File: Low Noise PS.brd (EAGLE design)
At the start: 228.6 x 101.6 mm, 64 parts, among them IC1 MAX6350SO08, IC2 OP27, IC3 LT1677, IC4 LT1677, IC5 MC79M12CDTG, IC6 MC78M12BDTG, Q1 MMBT2907AMMBTA56SOT23, Q2 MMBT5550SOT23, Q3 PMBF170, Q4 BSH201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

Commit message: Almost ready to print
1) "cosmetic" adjustments needed (mainly increasing clearance for traces
below SMD parts)
2) component values need to be adjusted and chosen
3) Silkscreen needs to be cleaned
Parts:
- added C26, C27, C28, C29: 22uF, rlc-jqi:1206
- added F1, F2: (no value), jqi-power-supply:FUSE1206
- moved R7 255.4 mm to (193.5, 41.5), turned to 90 degrees
- moved C7 245.1 mm to (200.0, 41.3)
- moved R2 243.3 mm to (205.4, 39.4)
- moved T1 241.9 mm to (187.7, 26.2), turned to 90 degrees
- moved C20 240.4 mm to (197.6, 41.3), turned to 270 degrees
- moved IC3 239.7 mm to (199.2, 35.6)
- moved R10 238.3 mm to (193.9, 35.4), turned to 90 degrees
- moved R1 238.0 mm to (206.8, 35.3), turned to 0 degrees
- moved C14 237.4 mm to (196.1, 28.6), turned to 270 degrees
- moved R9 236.2 mm to (192.7, 18.2), turned to 270 degrees
- moved R12 236.0 mm to (198.9, 28.6), turned to 90 degrees
- moved C11 235.8 mm to (201.9, 28.6), turned to 270 degrees
- moved C15 234.5 mm to (197.6, 32.4), turned to 0 degrees
- moved Q1 229.6 mm to (201.8, 23.6), turned to 0 degrees
- moved R11 228.8 mm to (194.9, 21.5), turned to 180 degrees
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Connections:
- new net N$22: F2.2, X1.2
- new net N$24: B2.AC2, F2.1
- net +15V: now also C26.2
- net -15V: now also C27.1
- net AGND: now also C26.1, C27.2, C28.1, C29.2
- net N$1: now also F1.1; no longer X1.1
- net N$5: now also F1.2, X1.1; no longer B2.AC2, X1.2
- net V+: now also C28.2
- net V-: now also C29.1
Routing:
- net V+: track 0.00 -> 53.8 mm, vias 0 -> 2
- net +12V: track 2.74 -> 51.5 mm
- net AGND: track 8.57 -> 55.8 mm, vias 2 -> 16
- net -12V: track 1.85 -> 35.5 mm
- net N$1: track 37.8 -> 12.3 mm
- net V-: track 0.00 -> 25.0 mm
- net N$15: track 0.00 -> 24.9 mm
- net -15V: track 0.00 -> 23.9 mm
- net N$5: track 40.4 -> 18.2 mm
- net N$22: track 0.00 -> 18.4 mm
- net N$17: track 3.10 -> 18.0 mm
- net N$24: track 0.00 -> 14.3 mm
- net N$19: track 0.00 -> 12.8 mm
- net N$7: track 0.00 -> 12.7 mm
- net N$14: track 0.00 -> 10.5 mm
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- added copper zone on layer 1, net +15V
- added copper zone on layer 16, net +15V
- added copper zone on layer 1, net -15V
- added copper zone on layer 16, net -15V
- added copper zone on layer 1, net AGND
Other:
- board text removed: "+5V"

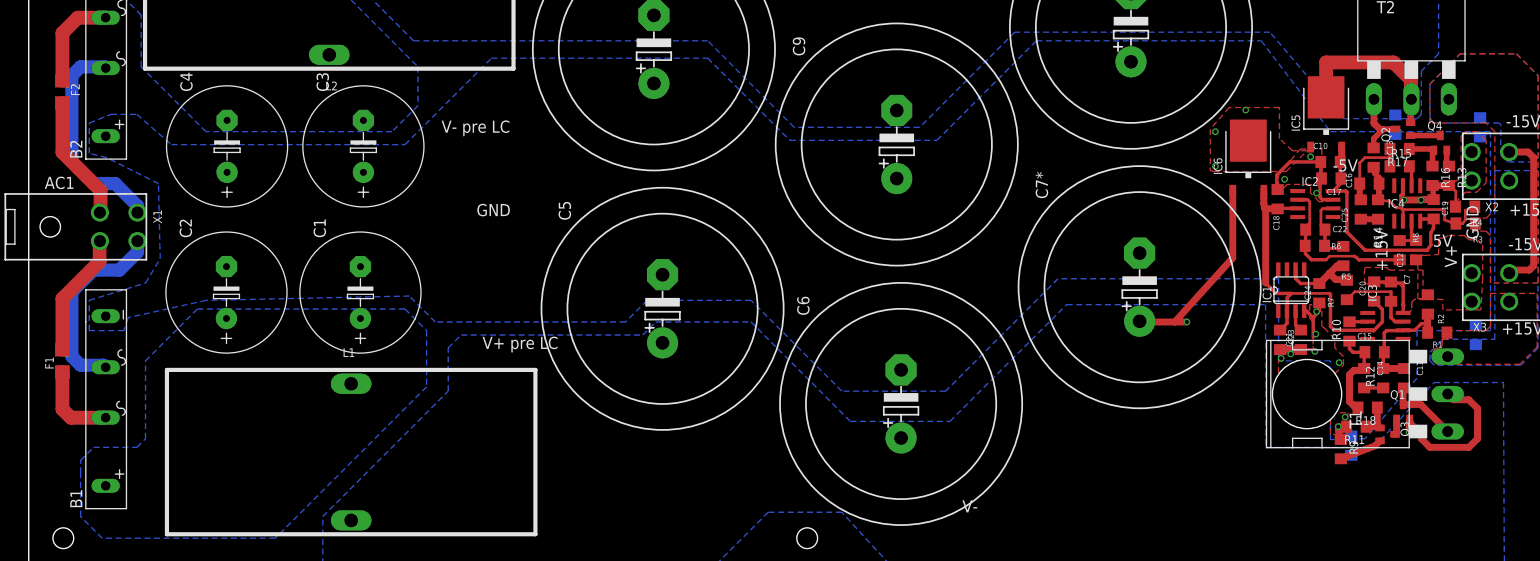
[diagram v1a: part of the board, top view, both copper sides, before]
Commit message: Version for LPKF printing.
Most resistor/capacitor values are not final.
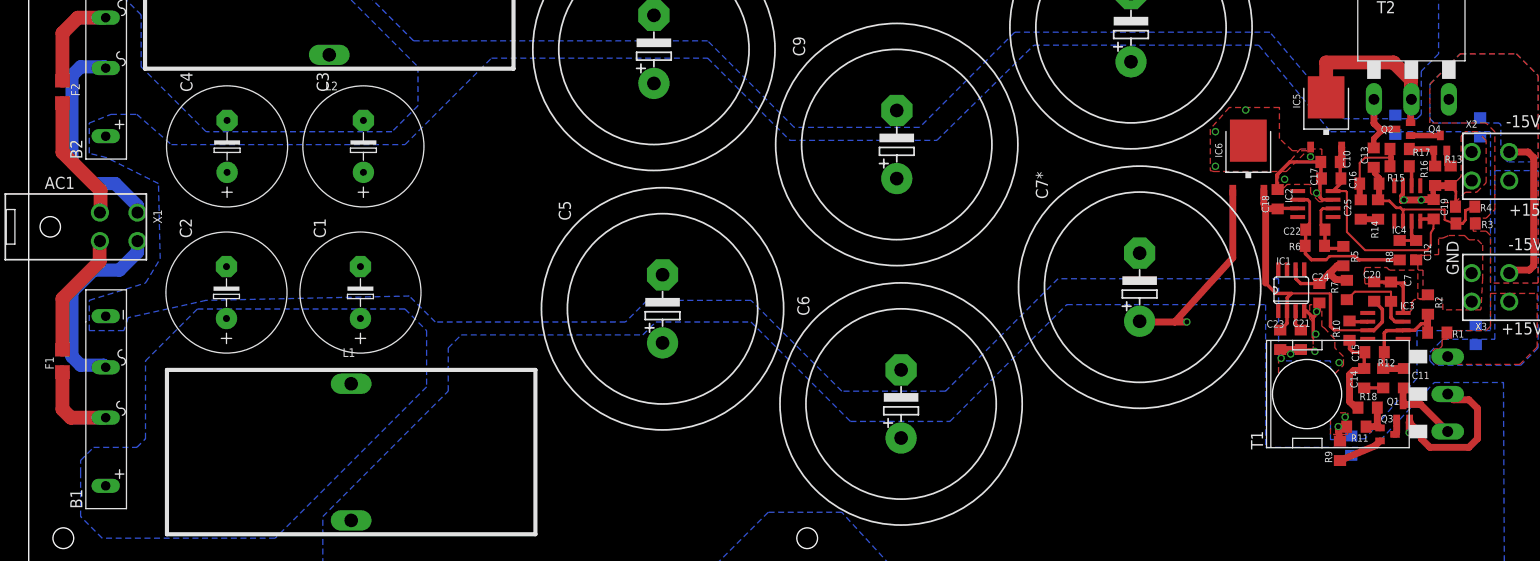
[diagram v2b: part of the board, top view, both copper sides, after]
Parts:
- moved R16 0.38 mm to (206.5, 58.3)
- moved R9 0.28 mm to (192.5, 17.9)
- moved R13 0.25 mm to (208.8, 58.3)
- moved R10 0.13 mm to (193.9, 35.6)
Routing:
- net AGND: track 55.8 -> 56.6 mm
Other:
- board text removed: "-5V"
- board text removed: "5V"
- board text removed: "V+"
- board text removed: "V+ pre LC"
- board text removed: "V-"
- board text removed: "V- pre LC"

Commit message: BOM and part attributes adjusted
This commit is not quite the final one:  a performance test must be done
before putting it into production. Also it might be useful to reorder
part names to make assembly easy.
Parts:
- C14, C25: value 220p -> 680p
- C15, C16: value 220p -> DNP
- C21, C22: value 1u -> 2.2u
- R10, R12, R14, R15: value 10k -> 1.5k
- R11, R16: value 10k -> DNP
- R17, R18: value 10k -> 0
- R5, R6: value 100k -> 10k
- renumbered C10* to C30, C7* to C31

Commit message: Change in component values. Not final version!
After assembling commit 290fa40aa6a372085 the board oscillates.
Changing all DNP resistors and all 0 Ohm resistors to 1.5K Ohm makes the
positive regulator stable under 6 Ohm load. The negative section is
still unstable. Some final value adjustment will be required to ensure
unconditional stability (with enough margin to account for the variation
of capacitor values with temperature.
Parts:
- R11, R16: value DNP -> 1.5k
- R17, R18: value 0 -> 1.5k
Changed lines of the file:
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@@
 <attribute name="DIGIKEY" value="541-1.5KECT-ND" x="193.929" y="35.56" size="1.778" layer="27" rot="R90" display="off"/>
 </element>
-<element name="R11" library="rcl" package="R1206" value="DNP" x="194.945" y="21.463" smashed="yes" rot="R180">
+<element name="R11" library="rcl" package="R1206" value="1.5k" x="194.945" y="21.463" smashed="yes" rot="R180">
 <attribute name="NAME" x="196.723" y="20.32" size="1.0668" layer="25" rot="R180"/>
 <attribute name="VALUE" x="196.215" y="24.003" size="1.27" layer="27" rot="R180"/>
+<attribute name="DIGIKEY" value="541-1.5KECT-ND" x="194.945" y="21.463" size="1.778" layer="27" rot="R180" display="off"/>
 </element>
 <element name="R12" library="rcl" package="R1206" value="1.5k" x="198.882" y="28.575" smashed="yes" rot="R90">
@@
 <attribute name="DIGIKEY" value="541-1.5KECT-ND" x="201.295" y="59.69" size="1.778" layer="27" display="off"/>
 </element>
-<element name="R16" library="rcl" package="R1206" value="DNP" x="206.502" y="58.293" smashed="yes" rot="R270">
+<element name="R16" library="rcl" package="R1206" value="1.5k" x="206.502" y="58.293" smashed="yes" rot="R270">
 <attribute name="NAME" x="204.343" y="60.579" size="1.0668" layer="25" rot="R270"/>
 <attribute name="VALUE" x="203.962" y="59.563" size="1.27" layer="27" rot="R270"/>
+<attribute name="DIGIKEY" value="541-1.5KECT-ND" x="206.502" y="58.293" size="1.778" layer="27" rot="R270" display="off"/>
 </element>
-<element name="R17" library="rcl" package="R1206" value="0" x="201.295" y="62.23" smashed="yes" rot="R180">
+<element name="R17" library="rcl" package="R1206" value="1.5k" x="201.295" y="62.23" smashed="yes" rot="R180">
 <attribute name="NAME" x="203.2" y="61.214" size="1.0668" layer="25"/>
 <attribute name="VALUE" x="202.565" y="64.77" size="1.27" layer="27" rot="R180"/>
-<attribute name="DIGIKEY" value="RMCF1206ZT0R00CT-ND" x="201.295" y="62.23" size="1.778" layer="27" rot="R180" display="off"/>
+<attribute name="DIGIKEY" value="541-1.5KECT-ND" x="201.295" y="62.23" size="1.778" layer="27" rot="R180" display="off"/>
 </element>
-<element name="R18" library="rcl" package="R1206" value="0" x="196.596" y="24.257" smashed="yes" rot="R180">
+<element name="R18" library="rcl" package="R1206" value="1.5k" x="196.596" y="24.257" smashed="yes" rot="R180">
 <attribute name="NAME" x="197.993" y="26.416" size="1.0668" layer="25" rot="R180"/>
 <attribute name="VALUE" x="197.866" y="26.797" size="1.27" layer="27" rot="R180"/>
-<attribute name="DIGIKEY" value="RMCF1206ZT0R00CT-ND" x="196.596" y="24.257" size="1.778" layer="27" rot="R180" display="off"/>
+<attribute name="DIGIKEY" value="541-1.5KECT-ND" x="196.596" y="24.257" size="1.778" layer="27" rot="R180" display="off"/>
 </element>
 <element name="F1" library="jqi-power-supply" package="FUSE1206" value="" x="4.953" y="31.115" smashed="yes" rot="R90">

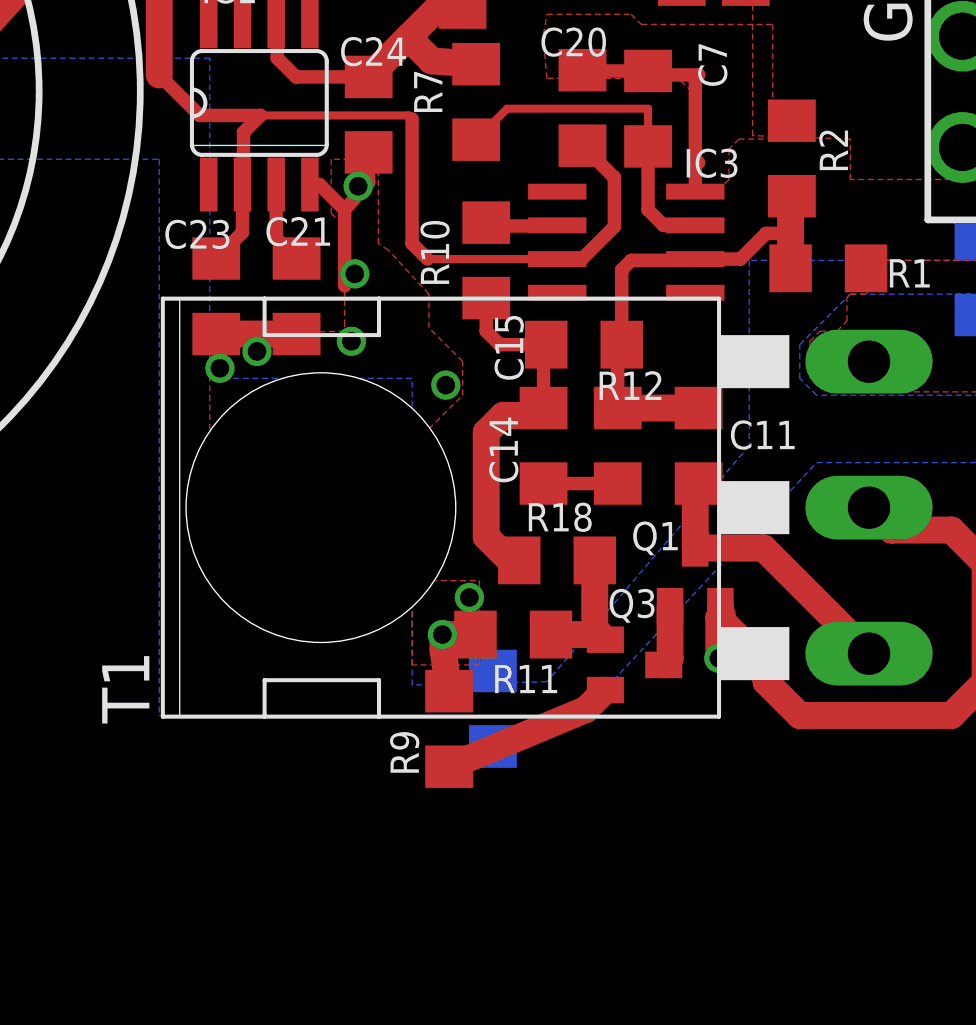
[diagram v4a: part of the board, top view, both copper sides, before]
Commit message: Moved capacitor
To avoid collision with transistor on the bottom side.
Also a resistor has been rotated to reduce a trace lenght
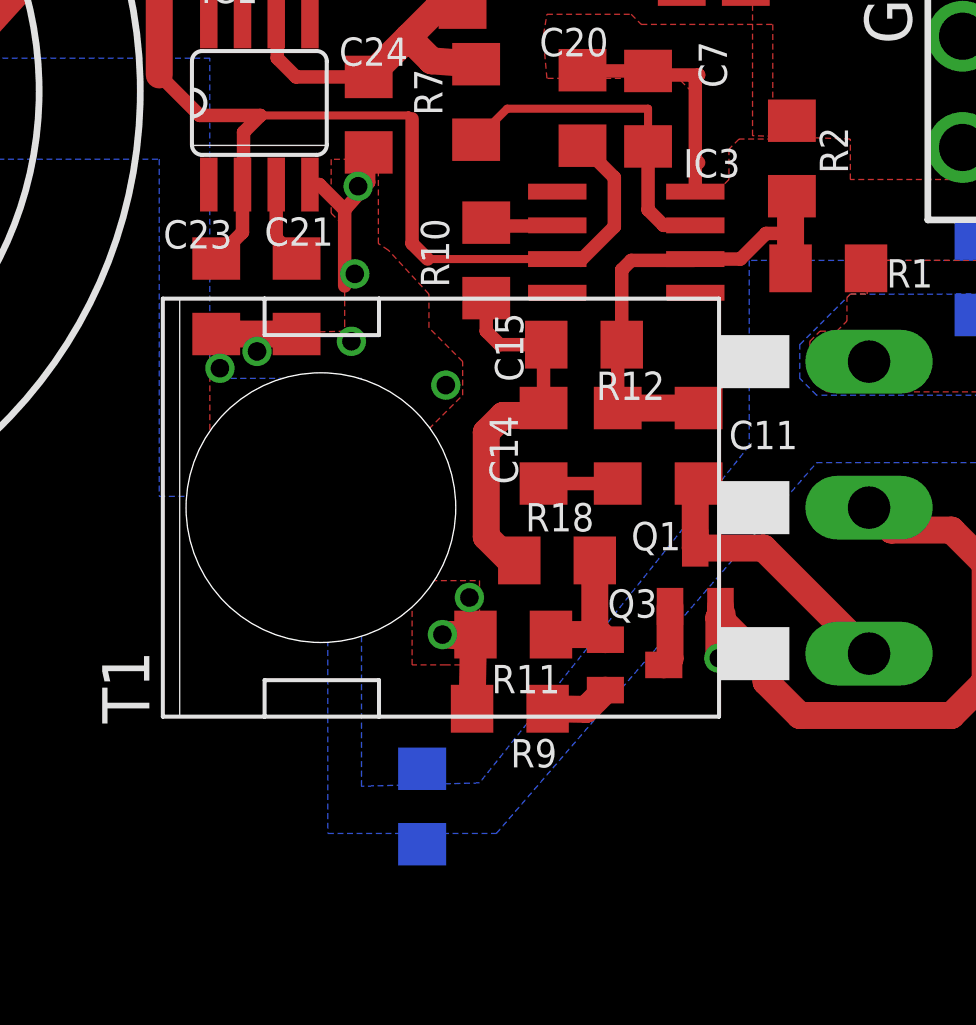
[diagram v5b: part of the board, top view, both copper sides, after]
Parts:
- moved C28 4.55 mm to (191.5, 15.0)
- moved R9 2.41 mm to (194.8, 18.7), turned to 0 degrees
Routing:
- net N$34: track 6.62 -> 2.48 mm
- net AGND: track 56.6 -> 58.3 mm
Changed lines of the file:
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@@
 <grid distance="0.025" unitdist="inch" unit="inch" style="dots" multiple="1" display="yes" altdistance="0.005" altunitdist="inch" altunit="inch"/>
 <layers>
-<layer number="1" name="Top" color="4" fill="1" visible="no" active="yes"/>
-<layer number="2" name="Route2" color="1" fill="3" visible="no" active="yes"/>
+<layer number="1" name="Top" color="4" fill="1" visible="yes" active="yes"/>
+<layer number="2" name="Route2" color="1" fill="3" visible="yes" active="yes"/>
 <layer number="3" name="Route3" color="4" fill="3" visible="no" active="no"/>
 <layer number="4" name="Route4" color="1" fill="4" visible="no" active="no"/>
@@
 <layer number="13" name="Route13" color="4" fill="5" visible="no" active="no"/>
 <layer number="14" name="Route14" color="1" fill="6" visible="no" active="no"/>
-<layer number="15" name="Route15" color="4" fill="6" visible="no" active="yes"/>
-<layer number="16" name="Bottom" color="1" fill="1" visible="no" active="yes"/>
+<layer number="15" name="Route15" color="4" fill="6" visible="yes" active="yes"/>
+<layer number="16" name="Bottom" color="1" fill="1" visible="yes" active="yes"/>
 <layer number="17" name="Pads" color="2" fill="1" visible="yes" active="yes"/>
 <layer number="18" name="Vias" color="2" fill="1" visible="yes" active="yes"/>
@@
 <layer number="21" name="tPlace" color="7" fill="1" visible="yes" active="yes"/>
 <layer number="22" name="bPlace" color="7" fill="1" visible="no" active="yes"/>
-<layer number="23" name="tOrigins" color="15" fill="1" visible="no" active="yes"/>
-<layer number="24" name="bOrigins" color="15" fill="1" visible="no" active="yes"/>
+<layer number="23" name="tOrigins" color="15" fill="1" visible="yes" active="yes"/>
+<layer number="24" name="bOrigins" color="15" fill="1" visible="yes" active="yes"/>
 <layer number="25" name="tNames" color="7" fill="1" visible="yes" active="yes"/>
 <layer number="26" name="bNames" color="7" fill="1" visible="no" active="yes"/>
@@
 <attribute name="DIGIKEY" value="MMBT2907AFSCT-ND" x="199.517" y="20.32" size="1.778" layer="27" rot="R270" display="off"/>
 </element>
-<element name="R9" library="rcl" package="R1206" value="10k" x="192.532" y="17.907" smashed="yes" rot="R270">
-<attribute name="NAME" x="191.389" y="16.129" size="1.0668" layer="25" rot="R90"/>
-<attribute name="VALUE" x="189.992" y="19.177" size="1.27" layer="27" rot="R270"/>
-<attribute name="DIGIKEY" value="RNCP1206FTD10K0CT-ND" x="192.532" y="17.907" size="1.778" layer="27" rot="R270" display="off"/>
+<element name="R9" library="rcl" package="R1206" value="10k" x="194.818" y="18.669" smashed="yes">
+<attribute name="NAME" x="196.596" y="17.526" size="1.0668" layer="25" rot="R180"/>
+<attribute name="VALUE" x="193.548" y="16.129" size="1.27" layer="27"/>
+<attribute name="DIGIKEY" value="RNCP1206FTD10K0CT-ND" x="194.818" y="18.669" size="1.778" layer="27" display="off"/>
 </element>
 <element name="R10" library="rcl" package="R1206" value="1.5k" x="193.929" y="35.56" smashed="yes" rot="R90">
@@
 <attribute name="VALUE" x="215.646" y="67.945" size="0.889" layer="28" rot="MR270"/>
 </element>
-<element name="C28" library="rlc-jqi" package="1206" value="22uF" x="194.183" y="18.669" smashed="yes" rot="MR270">
-<attribute name="DIGIKEY" value="445-8045-1-ND" x="194.183" y="18.669" size="1.778" layer="28" rot="MR270" display="off"/>
-<attribute name="NAME" x="192.278" y="21.209" size="0.889" layer="26" rot="MR270"/>
-<attribute name="VALUE" x="196.723" y="21.209" size="0.889" layer="28" rot="MR270"/>
+<element name="C28" library="rlc-jqi" package="1206" value="22uF" x="191.516" y="14.986" smashed="yes" rot="MR270">
+<attribute name="DIGIKEY" value="445-8045-1-ND" x="191.516" y="14.986" size="1.778" layer="28" rot="MR270" display="off"/>
+<attribute name="NAME" x="189.611" y="17.526" size="0.889" layer="26" rot="MR270"/>
+<attribute name="VALUE" x="194.056" y="17.526" size="0.889" layer="28" rot="MR270"/>
 </element>
 <element name="C29" library="rlc-jqi" package="1206" value="22uF" x="200.66" y="65.786" smashed="yes" rot="MR270">
@@
 <vertex x="203.835" y="35.56"/>
 <vertex x="203.835" y="28.575"/>
-<vertex x="196.215" y="19.685"/>
-<vertex x="191.135" y="19.558"/>
-<vertex x="191.135" y="31.115"/>
+<vertex x="193.675" y="15.875"/>
+<vertex x="189.23" y="15.748"/>
+<vertex x="189.23" y="31.115"/>
 <vertex x="183.515" y="31.115"/>
 <vertex x="183.515" y="43.18"/>
@@
 </polygon>
 <via x="192.278" y="21.463" extent="1-16" drill="0.7"/>
-<wire x1="192.532" y1="19.329" x2="192.303" y2="20.853" width="1.016" layer="1"/>
-<wire x1="192.303" y1="20.853" x2="192.278" y2="21.463" width="1.016" layer="1"/>
+<wire x1="193.396" y1="18.669" x2="193.446" y2="21.361" width="1.016" layer="1"/>
+<wire x1="193.446" y1="21.361" x2="192.278" y2="21.463" width="1.016" layer="1"/>
 <wire x1="193.523" y1="21.463" x2="192.278" y2="21.463" width="1.016" layer="1"/>
 <via x="193.294" y="22.86" extent="1-16" drill="0.7"/>
@@
 <vertex x="152.4" y="39.37"/>
 <vertex x="181.61" y="39.37"/>
-<vertex x="181.61" y="18.415"/>
-<vertex x="197.485" y="18.415"/>
+<vertex x="181.61" y="26.67"/>
+<vertex x="187.96" y="26.67"/>
+<vertex x="187.96" y="13.97"/>
+<vertex x="194.31" y="13.97"/>
 <vertex x="206.375" y="27.94"/>
 <vertex x="216.535" y="27.94"/>
@@
 <contactref element="Q3" pad="2"/>
 <contactref element="R9" pad="2"/>
-<wire x1="192.532" y1="16.485" x2="197.691" y2="18.644" width="1.016" layer="1"/>
+<wire x1="196.24" y1="18.669" x2="197.691" y2="18.644" width="1.016" layer="1"/>
 <wire x1="197.691" y1="18.644" x2="198.417" y2="19.37" width="1.016" layer="1"/>
 </signal>
